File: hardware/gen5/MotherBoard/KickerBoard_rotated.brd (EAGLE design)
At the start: 144.2 x 141.8 mm, 155 parts

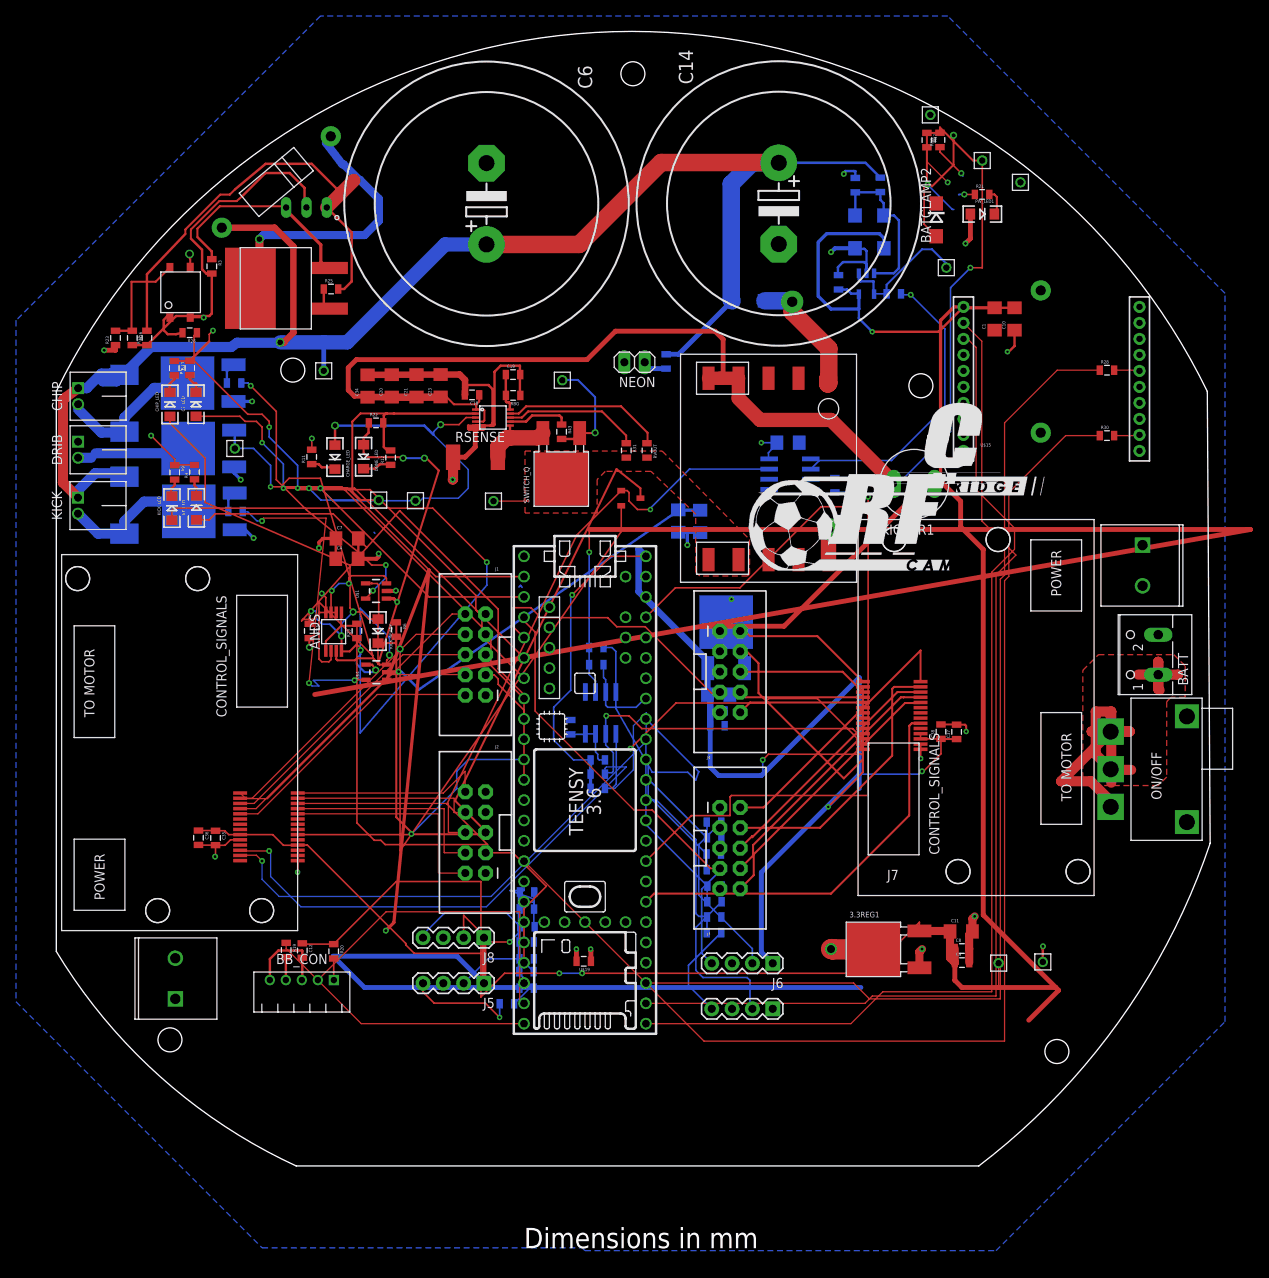
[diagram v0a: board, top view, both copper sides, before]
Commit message: rotating the entire center piece
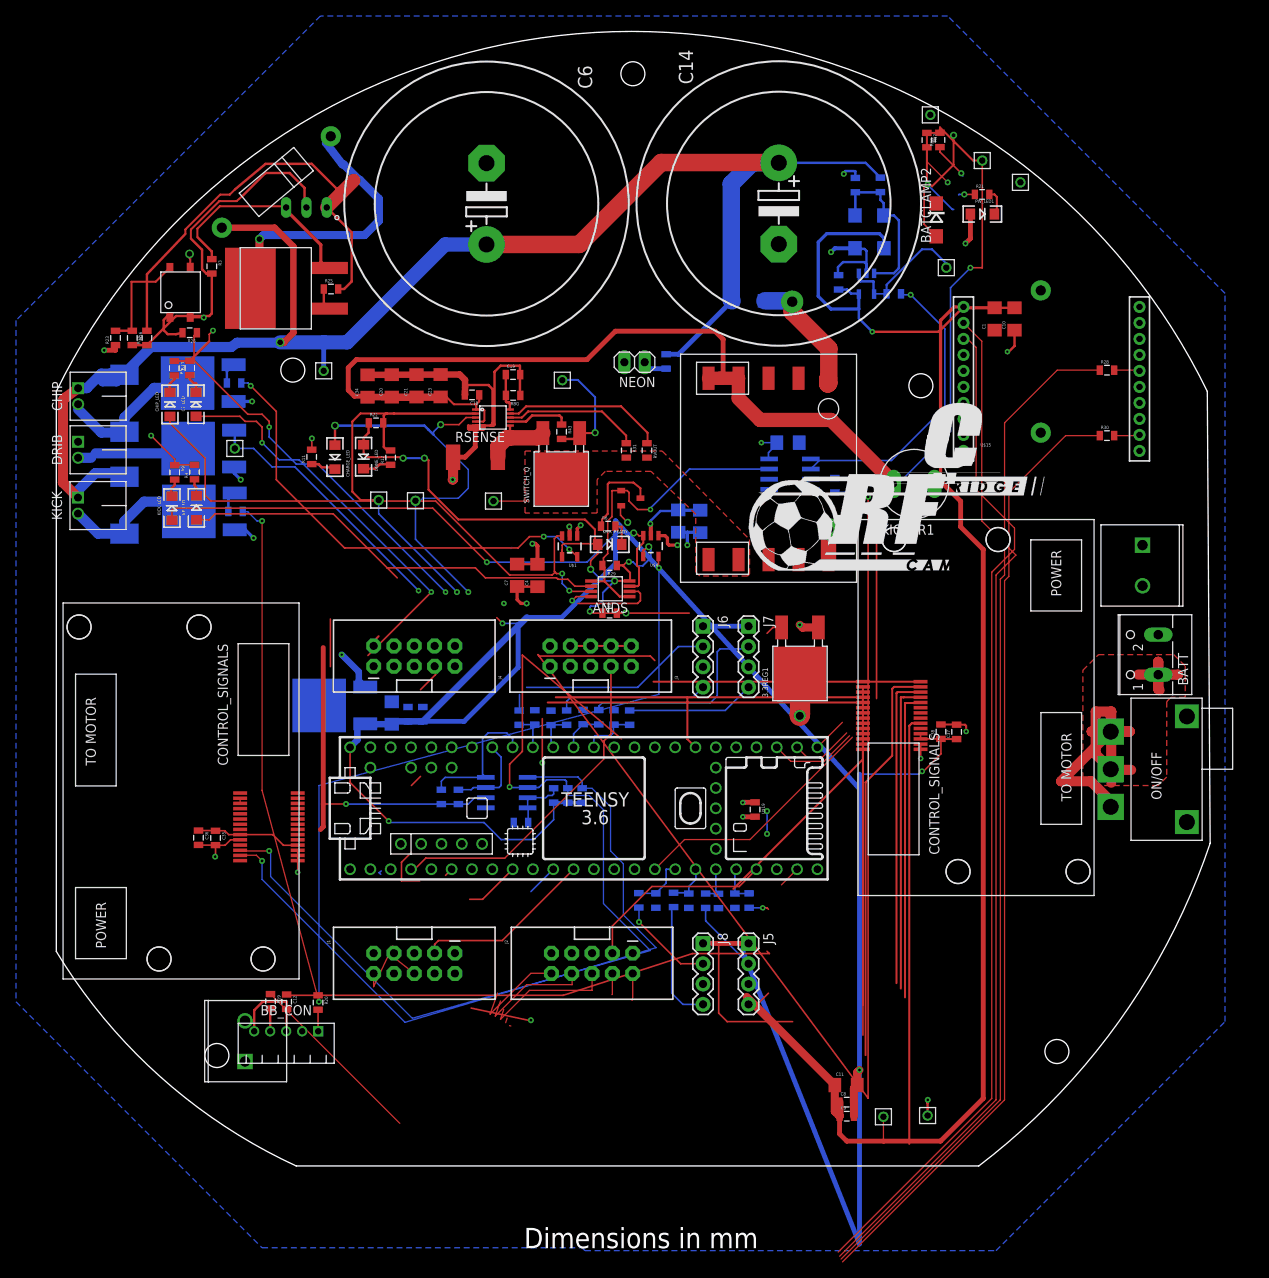
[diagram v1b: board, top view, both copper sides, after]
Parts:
- moved 5REG 51.9 mm to (30.8, 61.0), turned to 180 degrees
- moved J7 47.9 mm to (84.5, 70.9), turned to 270 degrees
- moved J6 43.0 mm to (78.8, 70.9), turned to 270 degrees
- moved C41 40.9 mm to (39.9, 60.1), turned to 90 degrees
- moved J4 39.5 mm to (42.7, 67.2), turned to 90 degrees
- moved J1 39.3 mm to (42.7, 28.8), turned to 270 degrees
- moved C39 38.7 mm to (41.9, 59.9), turned to 90 degrees
- moved U$4 37.8 mm to (72.2, 81.0), turned to 180 degrees
- moved C15 37.6 mm to (67.1, 72.6), turned to 0 degrees
- moved C40 36.9 mm to (43.7, 59.9), turned to 90 degrees
- moved 3.3REG1 35.7 mm to (90.9, 65.0), turned to 90 degrees
- moved ANDS 35.0 mm to (67.2, 75.6), turned to 0 degrees
- moved J5 33.4 mm to (84.5, 31.3), turned to 270 degrees
- moved R50 32.9 mm to (84.5, 36.7), turned to 270 degrees
- moved R29 32.6 mm to (67.1, 78.5), turned to 180 degrees
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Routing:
- net 3.3V: track 614.8 -> 396.2 mm
- net 12V: track 164.1 -> 39.7 mm
- net N$2: track 40.9 -> 152.2 mm
- net KICK_REF: track 75.0 -> 164.3 mm
- net COMP_OUT: track 124.7 -> 41.0 mm
- net N$14: track 93.9 -> 11.3 mm
- net 12VGND: track 257.4 -> 194.1 mm
- net GND: track 156.0 -> 104.5 mm
- net CHIP_ENABLE: track 107.5 -> 61.6 mm
- net 5V: track 311.9 -> 356.8 mm
- net BB_IN: track 40.4 -> 2.77 mm
- net DIR0: track 36.6 -> 0.63 mm
- net ENABLE0: track 35.1 -> 0.07 mm
- net FAULT0: track 34.4 -> 0.14 mm
- net BREN0: track 35.8 -> 3.09 mm
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
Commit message: ripup of all redundant wires
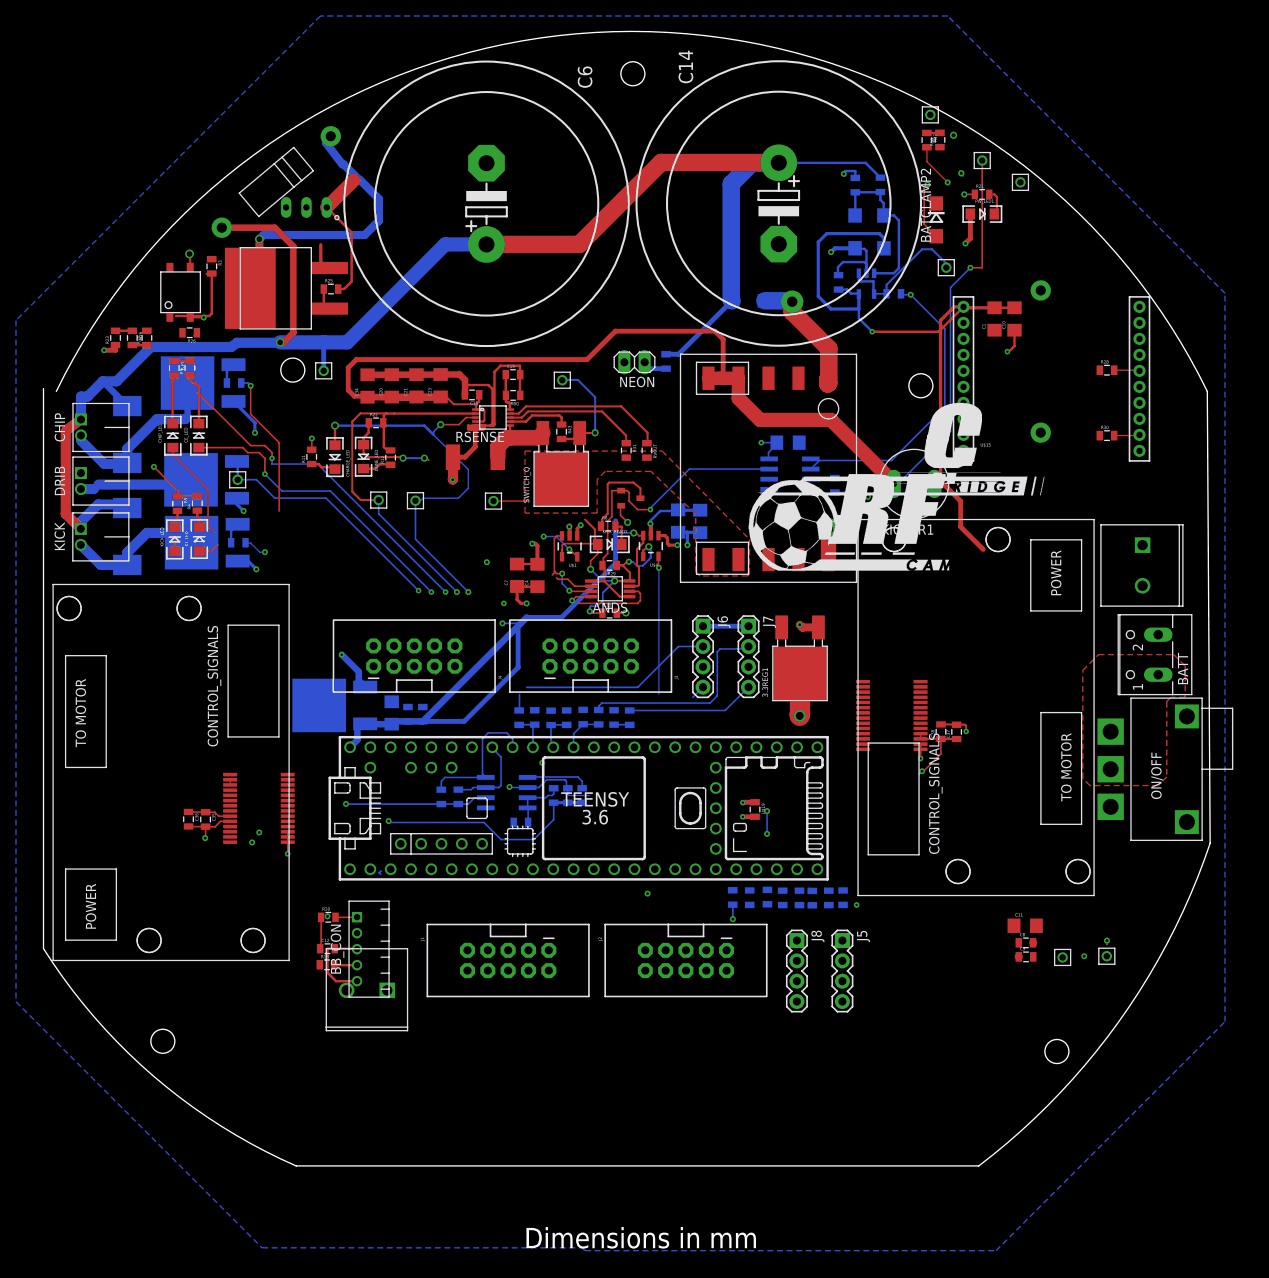
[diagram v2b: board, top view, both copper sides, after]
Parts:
- moved C11 30.0 mm to (119.0, 33.5)
- moved C9 30.0 mm to (119.1, 29.6)
- moved 3.3V 30.0 mm to (123.7, 29.5)
- moved C8 30.0 mm to (119.1, 31.4)
- moved GND 30.0 mm to (129.2, 29.7)
- moved U$13 19.9 mm to (39.3, 25.4), turned to 180 degrees
- moved BB_CON 13.6 mm to (35.5, 30.6), turned to 90 degrees
- moved J5 11.7 mm to (96.2, 31.6)
- moved J8 11.7 mm to (90.5, 31.6)
- moved R49 11.7 mm to (88.7, 37.0)
- moved R50 11.7 mm to (96.3, 37.0)
- moved J1 11.7 mm to (54.4, 29.2)
- moved J2 11.7 mm to (76.6, 29.2)
- moved R48 11.7 mm to (86.8, 37.1)
- moved R51 11.7 mm to (94.5, 37.0)
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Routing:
- net 3.3V: track 396.2 -> 159.1 mm
- net 5V: track 356.8 -> 122.8 mm
- net KICK_REF: track 164.3 -> 5.09 mm
- net CTS: track 150.6 -> 0.00 mm
- net RTS: track 138.8 -> 0.02 mm
- net RX: track 136.5 -> 0.00 mm
- net N$2: track 152.2 -> 20.2 mm
- net TX: track 130.6 -> 0.51 mm
- net SCL-H: track 131.2 -> 12.6 mm
- net SDA-H: track 103.1 -> 9.82 mm
- net BAT+: track 61.2 -> 0.00 mm
- net INT2: track 60.5 -> 0.00 mm
- net KICK: track 72.8 -> 13.2 mm
- net KICK_ENABLE: track 62.1 -> 7.40 mm
- net BATSENSE: track 103.7 -> 51.6 mm
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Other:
- board size 144.2 x 141.8 mm -> 145.8 x 141.8 mm

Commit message: ripping up
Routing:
- net GND: track 57.0 -> 81.4 mm
- net LOCKN0: track 0.00 -> 19.5 mm
- net SDA: track 17.3 -> 0.57 mm
- net SCL: track 10.8 -> 0.00 mm
- net 3.3V: track 159.1 -> 153.9 mm
- net M1QA-3OUT: track 5.35 -> 1.97 mm
- net M1QB-2OUT: track 4.87 -> 1.97 mm
- net M1QA-2OUT: track 4.89 -> 2.29 mm
- net DIR0: track 0.63 -> 0.00 mm
